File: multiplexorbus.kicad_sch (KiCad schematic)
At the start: 4 parts, among them U27 74LS138, U28 74LS138, U29 74LS137, U30 74LS137

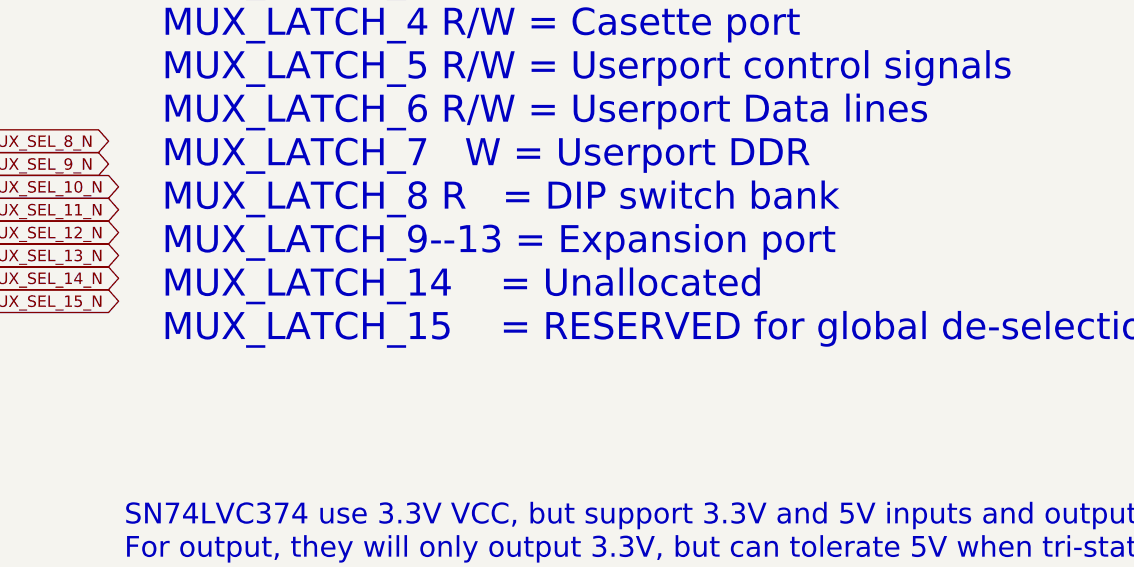
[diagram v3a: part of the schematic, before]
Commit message: add C64 keyboard connector on MUX bus #9
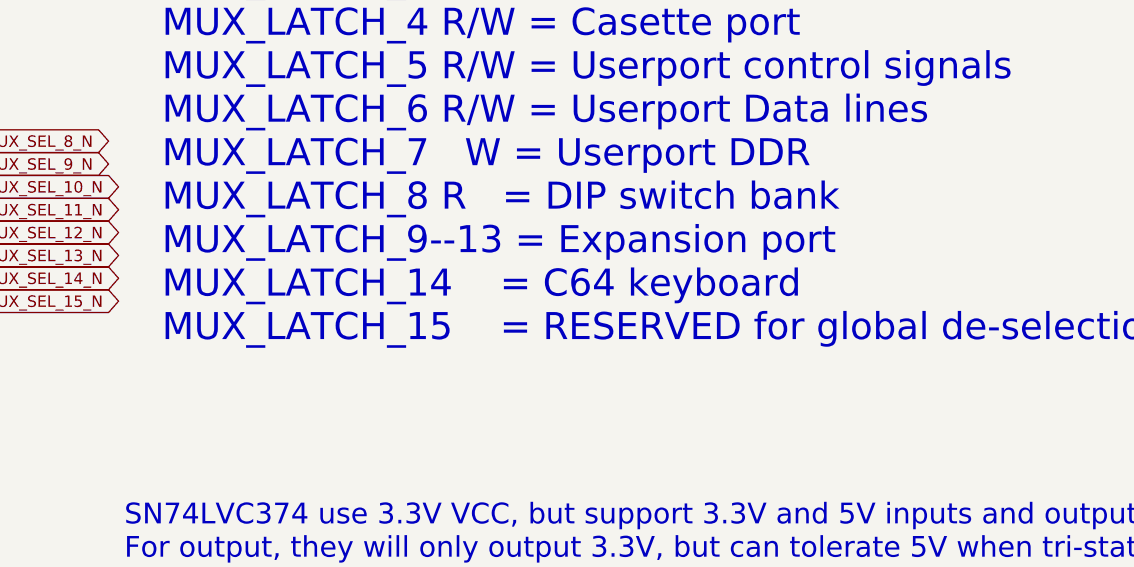
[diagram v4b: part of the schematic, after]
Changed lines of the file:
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@@
     (effects (font (size 2.3 2.3)) (justify left bottom))
   )
-  (text "Multiplexor Bus Register Allocation\n-----------------------------------\n\nMUX_LATCH_0 R/W = 34-pin floppy\nMUX_LATCH_1 R/W = IEC Serial\nMUX_LATCH_2 R/W = Joystick 1\nMUX_LATCH_3 R/W = Joystick 2\nMUX_LATCH_4 R/W = Casette port\nMUX_LATCH_5 R/W = Userport control signals\nMUX_LATCH_6 R/W = Userport Data lines\nMUX_LATCH_7   W = Userport DDR\nMUX_LATCH_8 R   = DIP switch bank\nMUX_LATCH_9--13 = Expansion port\nMUX_LATCH_14    = Unallocated\nMUX_LATCH_15    = RESERVED for global de-selection"
+  (text "Multiplexor Bus Register Allocation\n-----------------------------------\n\nMUX_LATCH_0 R/W = 34-pin floppy\nMUX_LATCH_1 R/W = IEC Serial\nMUX_LATCH_2 R/W = Joystick 1\nMUX_LATCH_3 R/W = Joystick 2\nMUX_LATCH_4 R/W = Casette port\nMUX_LATCH_5 R/W = Userport control signals\nMUX_LATCH_6 R/W = Userport Data lines\nMUX_LATCH_7   W = Userport DDR\nMUX_LATCH_8 R   = DIP switch bank\nMUX_LATCH_9--13 = Expansion port\nMUX_LATCH_14    = C64 keyboard\nMUX_LATCH_15    = RESERVED for global de-selection"
     (at 153.67 102.616 0)
     (effects (font (size 3 3)) (justify left bottom))

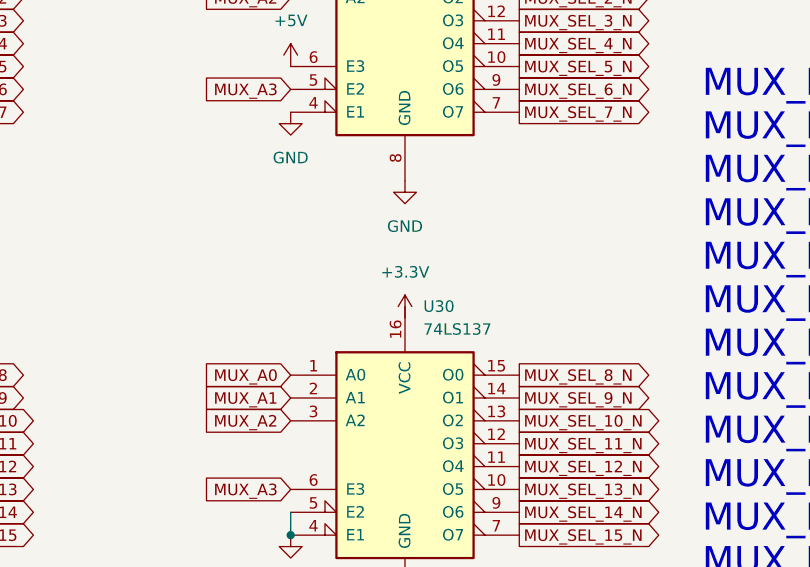
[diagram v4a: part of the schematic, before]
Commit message: more cart and mux bus layout
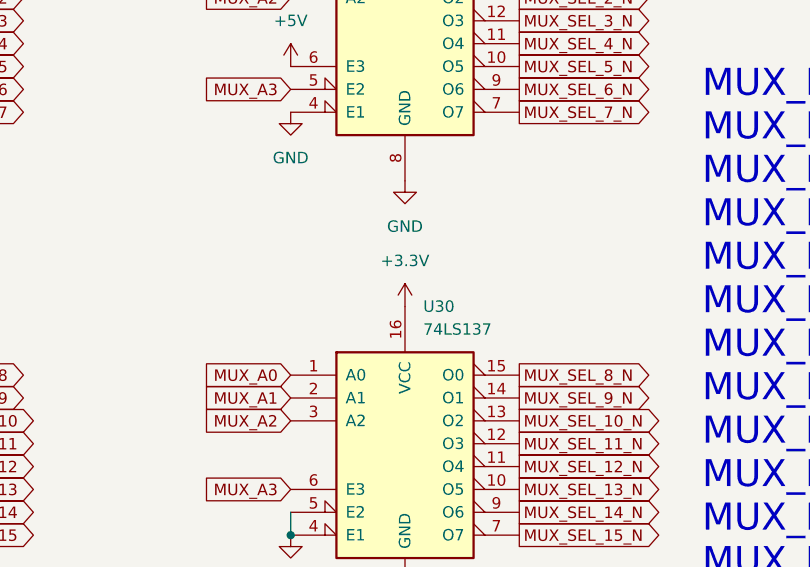
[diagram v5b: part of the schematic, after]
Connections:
- net +3V3: now also U30.16 (VCC)
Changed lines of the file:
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@@
     (pin "1")
   )
-  (symbol (lib_id "power:+3.3V") (at 120.65 73.66 0) (unit 1)
+  (symbol (lib_id "power:+3.3V") (at 120.65 72.39 0) (unit 1)
     (in_bom yes) (on_board yes) (fields_autoplaced)
-    (property "Reference" "#PWR0236" (id 0) (at 120.65 77.47 0)
+    (property "Reference" "#PWR0236" (id 0) (at 120.65 76.2 0)
       (effects (font (size 1.27 1.27)) hide)
     )
-    (property "Value" "+3.3V" (id 1) (at 120.65 68.58 0))
-    (property "Footprint" "" (id 2) (at 120.65 73.66 0)
+    (property "Value" "+3.3V" (id 1) (at 120.65 67.31 0))
+    (property "Footprint" "" (id 2) (at 120.65 72.39 0)
       (effects (font (size 1.27 1.27)) hide)
     )
-    (property "Datasheet" "" (id 3) (at 120.65 73.66 0)
+    (property "Datasheet" "" (id 3) (at 120.65 72.39 0)
       (effects (font (size 1.27 1.27)) hide)
     )

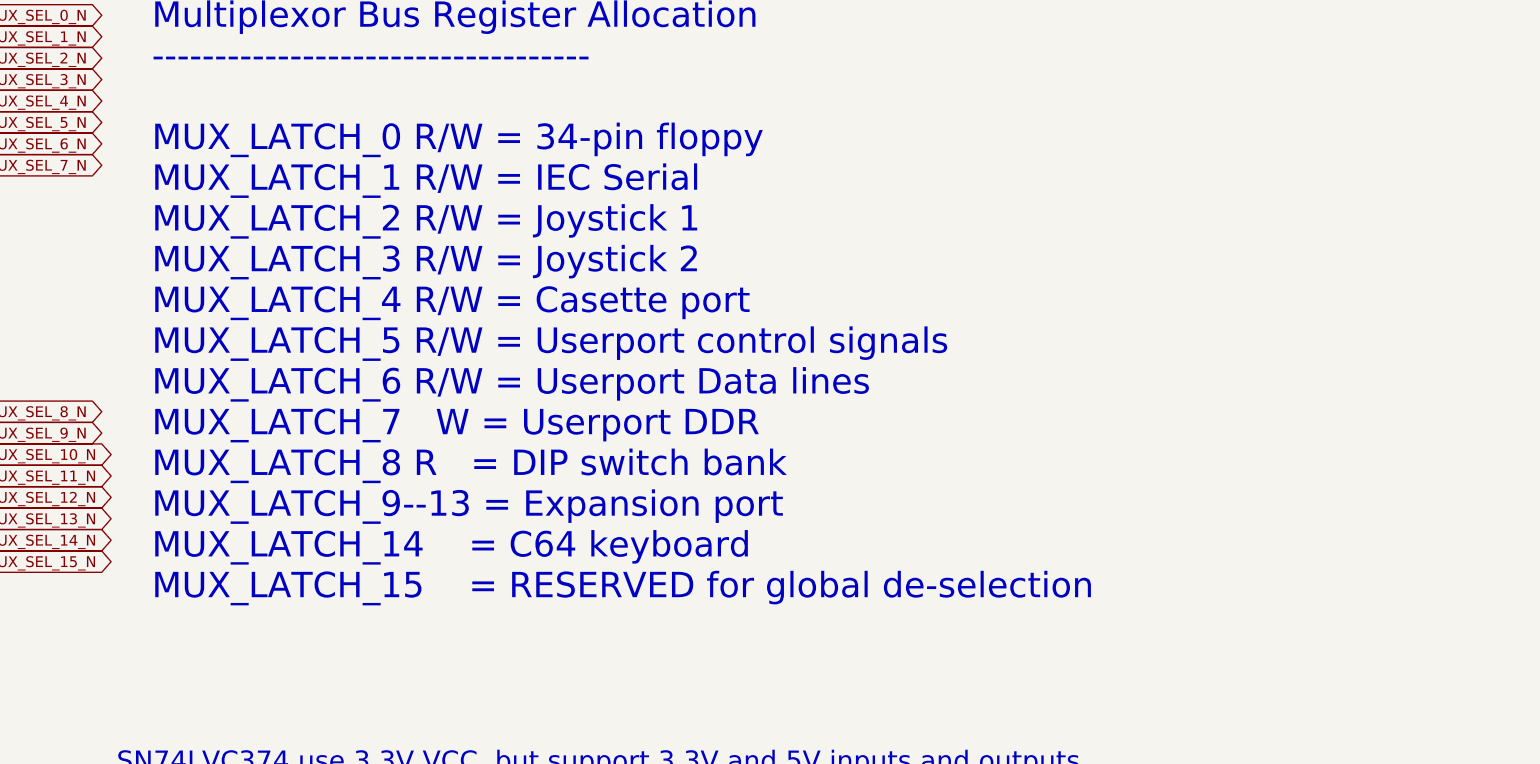
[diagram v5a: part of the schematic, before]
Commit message: renumber MUX registers to ease routing
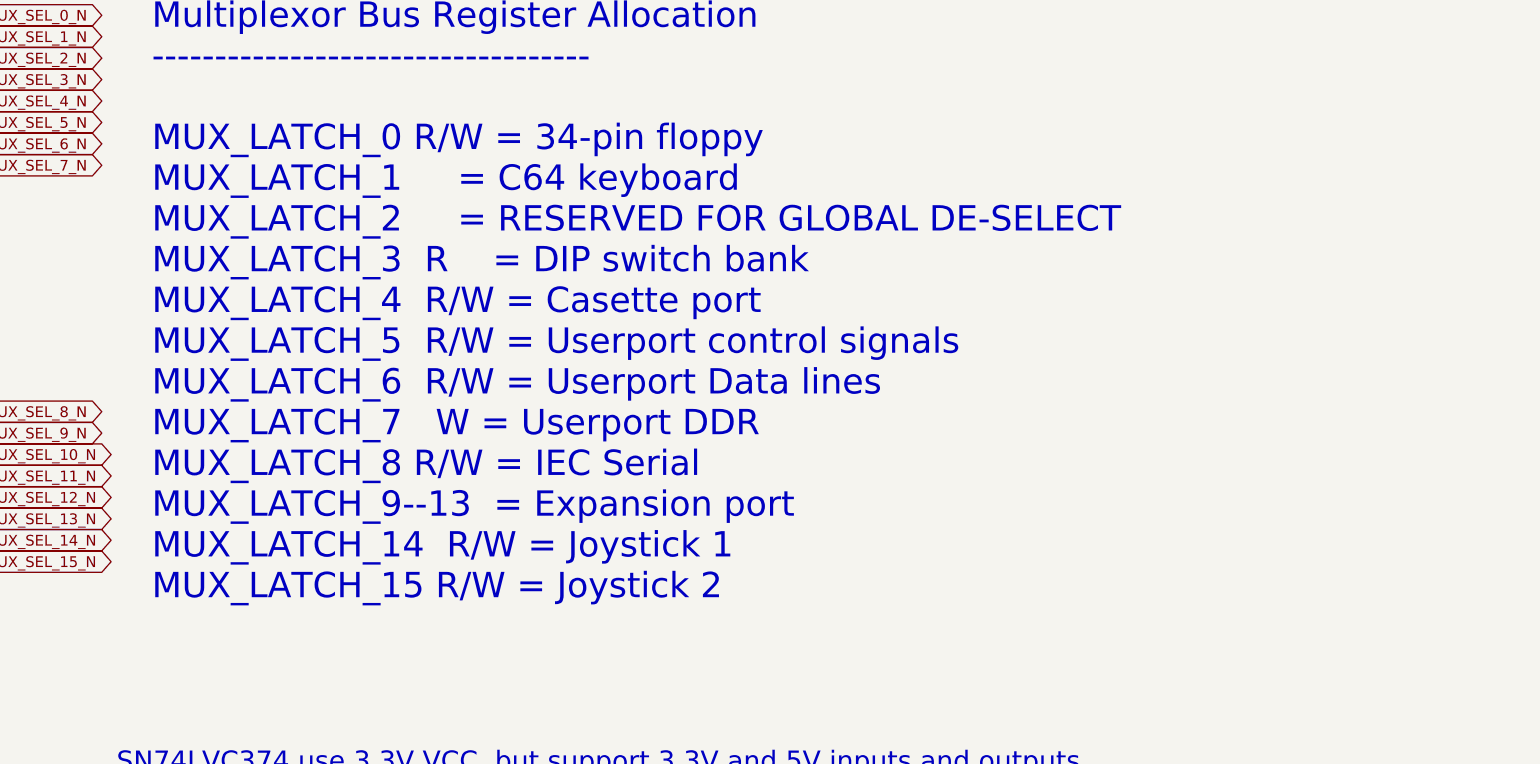
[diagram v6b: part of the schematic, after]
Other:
- note added: "Multiplexor Bus Register Allocation ----------------------------------- MUX_LATCH_0 R/W = 34-pin floppy MUX_LATCH_1 = C64 keyboard MUX_LATCH_2 = RESERVED FOR GLOBAL DE-SELECT MUX_LATCH_3 R = DIP switch bank MUX_LATCH_4 R/W = Casette port MUX_LATCH_5 R/W = Userport control signals MUX_LATCH_6 R/W = Userport Data lines MUX_LATCH_7 W = Userport DDR MUX_LATCH_8 R/W = IEC Serial MUX_LATCH_9--13 = Expa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"
- note removed: "Multiplexor Bus Register Allocation ----------------------------------- MUX_LATCH_0 R/W = 34-pin floppy MUX_LATCH_1 R/W = IEC Serial MUX_LATCH_2 R/W = Joystick 1 MUX_LATCH_3 R/W = Joystick 2 MUX_LATCH_4 R/W = Casette port MUX_LATCH_5 R/W = Userport control signals MUX_LATCH_6 R/W = Userport Data lines MUX_LATCH_7 W = Userport DDR MUX_LATCH_8 R = DIP switch bank MUX_LATCH_9--13 = Expansion port MU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"
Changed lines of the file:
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@@
     (effects (font (size 2.3 2.3)) (justify left bottom))
   )
-  (text "Multiplexor Bus Register Allocation\n-----------------------------------\n\nMUX_LATCH_0 R/W = 34-pin floppy\nMUX_LATCH_1 R/W = IEC Serial\nMUX_LATCH_2 R/W = Joystick 1\nMUX_LATCH_3 R/W = Joystick 2\nMUX_LATCH_4 R/W = Casette port\nMUX_LATCH_5 R/W = Userport control signals\nMUX_LATCH_6 R/W = Userport Data lines\nMUX_LATCH_7   W = Userport DDR\nMUX_LATCH_8 R   = DIP switch bank\nMUX_LATCH_9--13 = Expansion port\nMUX_LATCH_14    = C64 keyboard\nMUX_LATCH_15    = RESERVED for global de-selection"
+  (text "Multiplexor Bus Register Allocation\n-----------------------------------\n\nMUX_LATCH_0 R/W = 34-pin floppy\nMUX_LATCH_1     = C64 keyboard\nMUX_LATCH_2     = RESERVED FOR GLOBAL DE-SELECT\nMUX_LATCH_3  R    = DIP switch bank\nMUX_LATCH_4  R/W = Casette port\nMUX_LATCH_5  R/W = Userport control signals\nMUX_LATCH_6  R/W = Userport Data lines\nMUX_LATCH_7   W = Userport DDR\nMUX_LATCH_8 R/W = IEC Serial\nMUX_LATCH_9--13  = Expansion port\nMUX_LATCH_14  R/W = Joystick 1\nMUX_LATCH_15 R/W = Joystick 2\n"
     (at 153.67 102.616 0)
     (effects (font (size 3 3)) (justify left bottom))

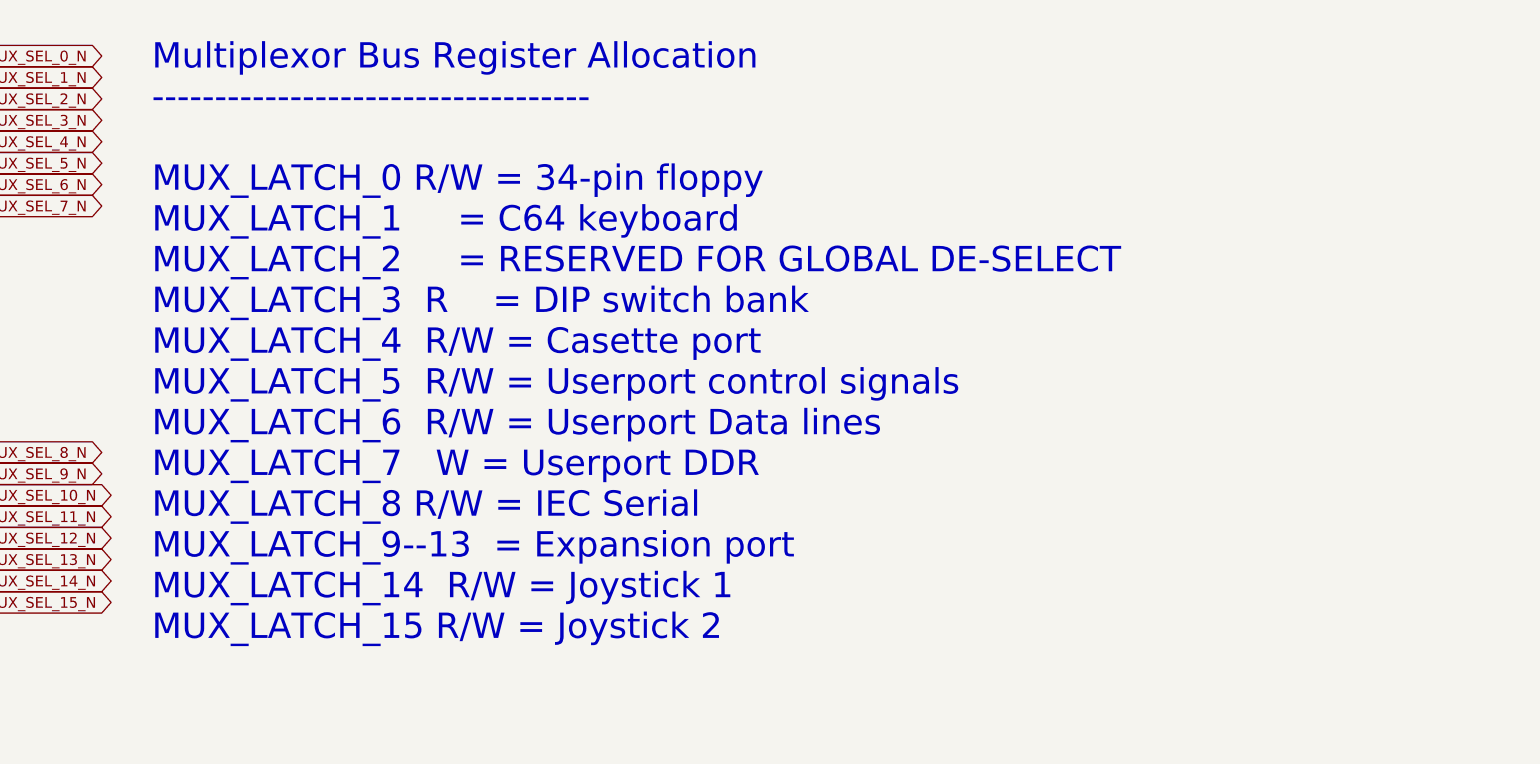
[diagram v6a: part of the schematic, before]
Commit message: switch DIP8 to DIP4 using spare pins on floppy MUX R unit
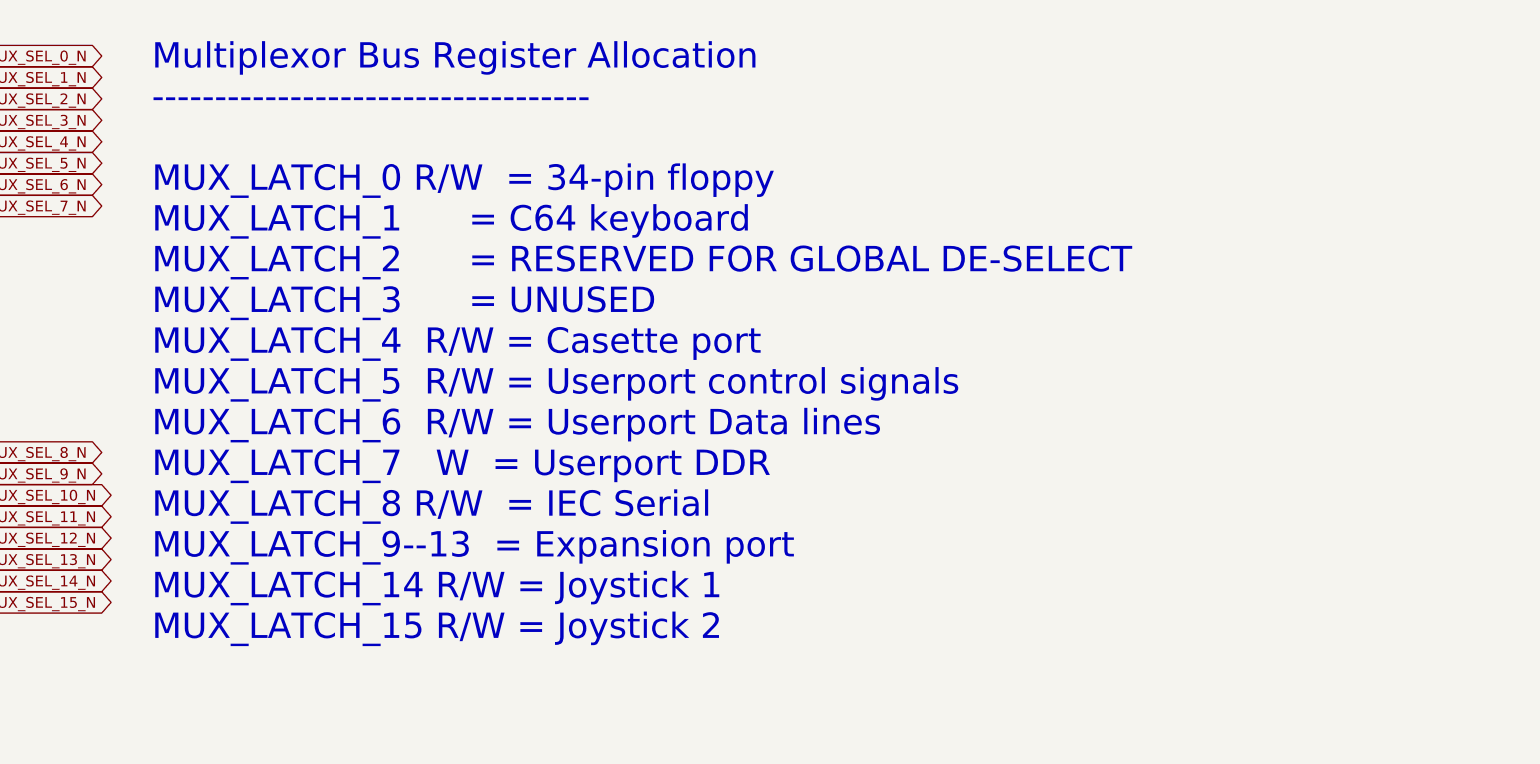
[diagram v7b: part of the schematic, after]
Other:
- note added: "Multiplexor Bus Register Allocation ----------------------------------- MUX_LATCH_0 R/W = 34-pin floppy MUX_LATCH_1 = C64 keyboard MUX_LATCH_2 = RESERVED FOR GLOBAL DE-SELECT MUX_LATCH_3 = UNUSED MUX_LATCH_4 R/W = Casette port MUX_LATCH_5 R/W = Userport control signals MUX_LATCH_6 R/W = Userport Data lines MUX_LATCH_7 W = Userport DDR MUX_LATCH_8 R/W = IEC Serial MUX_LATCH_9--13 = Expansion port 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"
- note removed: "Multiplexor Bus Register Allocation ----------------------------------- MUX_LATCH_0 R/W = 34-pin floppy MUX_LATCH_1 = C64 keyboard MUX_LATCH_2 = RESERVED FOR GLOBAL DE-SELECT MUX_LATCH_3 R = DIP switch bank MUX_LATCH_4 R/W = Casette port MUX_LATCH_5 R/W = Userport control signals MUX_LATCH_6 R/W = Userport Data lines MUX_LATCH_7 W = Userport DDR MUX_LATCH_8 R/W = IEC Serial MUX_LATCH_9--13 = Expa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"
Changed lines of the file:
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@@
     (effects (font (size 2.3 2.3)) (justify left bottom))
   )
-  (text "Multiplexor Bus Register Allocation\n-----------------------------------\n\nMUX_LATCH_0 R/W = 34-pin floppy\nMUX_LATCH_1     = C64 keyboard\nMUX_LATCH_2     = RESERVED FOR GLOBAL DE-SELECT\nMUX_LATCH_3  R    = DIP switch bank\nMUX_LATCH_4  R/W = Casette port\nMUX_LATCH_5  R/W = Userport control signals\nMUX_LATCH_6  R/W = Userport Data lines\nMUX_LATCH_7   W = Userport DDR\nMUX_LATCH_8 R/W = IEC Serial\nMUX_LATCH_9--13  = Expansion port\nMUX_LATCH_14  R/W = Joystick 1\nMUX_LATCH_15 R/W = Joystick 2\n"
+  (text "Multiplexor Bus Register Allocation\n-----------------------------------\n\nMUX_LATCH_0 R/W  = 34-pin floppy\nMUX_LATCH_1      = C64 keyboard\nMUX_LATCH_2      = RESERVED FOR GLOBAL DE-SELECT\nMUX_LATCH_3      = UNUSED\nMUX_LATCH_4  R/W = Casette port\nMUX_LATCH_5  R/W = Userport control signals\nMUX_LATCH_6  R/W = Userport Data lines\nMUX_LATCH_7   W  = Userport DDR\nMUX_LATCH_8 R/W  = IEC Serial\nMUX_LATCH_9--13  = Expansion port\nMUX_LATCH_14 R/W = Joystick 1\nMUX_LATCH_15 R/W = Joystick 2\n"
     (at 153.67 102.616 0)
     (effects (font (size 3 3)) (justify left bottom))

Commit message: re-do many labels and DRC fixes
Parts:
- U27, U28: footprint Package_DIP:DIP-16_W7.62mm -> snapeda:DIP-16_LS_Family
- U29, U30: footprint Package_DIP:DIP-16_W7.62mm -> snapeda:DIP-16_LVC_Family
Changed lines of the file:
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@@
       (effects (font (size 1.27 1.27)) (justify left))
     )
-    (property "Footprint" "Package_DIP:DIP-16_W7.62mm" (id 2) (at 120.65 87.63 0)
+    (property "Footprint" "snapeda:DIP-16_LVC_Family" (id 2) (at 120.65 87.63 0)
       (effects (font (size 1.27 1.27)) hide)
     )
@@
       (effects (font (size 1.27 1.27)) (justify left))
     )
-    (property "Footprint" "Package_DIP:DIP-16_W7.62mm" (id 2) (at 120.65 40.64 0)
+    (property "Footprint" "snapeda:DIP-16_LVC_Family" (id 2) (at 120.65 40.64 0)
       (effects (font (size 1.27 1.27)) hide)
     )
@@
       (effects (font (size 1.27 1.27)) (justify left))
     )
-    (property "Footprint" "Package_DIP:DIP-16_W7.62mm" (id 2) (at 53.34 87.63 0)
+    (property "Footprint" "snapeda:DIP-16_LS_Family" (id 2) (at 53.34 87.63 0)
       (effects (font (size 1.27 1.27)) hide)
     )
@@
       (effects (font (size 1.27 1.27)) (justify left))
     )
-    (property "Footprint" "Package_DIP:DIP-16_W7.62mm" (id 2) (at 53.34 40.64 0)
-      (effects (font (size 1.27 1.27)) hide)
-    )
+    (property "Footprint" "snapeda:DIP-16_LS_Family" (id 2) (at 53.34 40.64 0)
+      (effects (font (size 1.27 1.27)) hide)
+    )
